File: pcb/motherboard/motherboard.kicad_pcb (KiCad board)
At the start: 4 copper layers, 99.1 x 39.4 mm, 90 parts, among them J1 DC_IN, J10 PSU, J11 HEADER-1x01, J12 HEADER-1x01, J13 USB-LED, J14 EXT, J15 EXT-PW, J16 EXT-I2C, J17 WIFI-GPIO, J2 USB-MINI-B, J3 DB PWR, J4 ICSP-USB, J5 Micro_SD, J6 PSU-SIG, J7 ICSP, J8 FRONT PANEL, J9 DB I/O, SW1 RESET, U1 ATMEGA2560-16AU, U2 DS3231M, U3 ATMEGA8U2-AU, U4 ATWINC1500-MR, U5 74X4050, U6 AP2112K-3.3, U7 74X4050, Y1 16.00 MHz, Y2 16.00 MHz

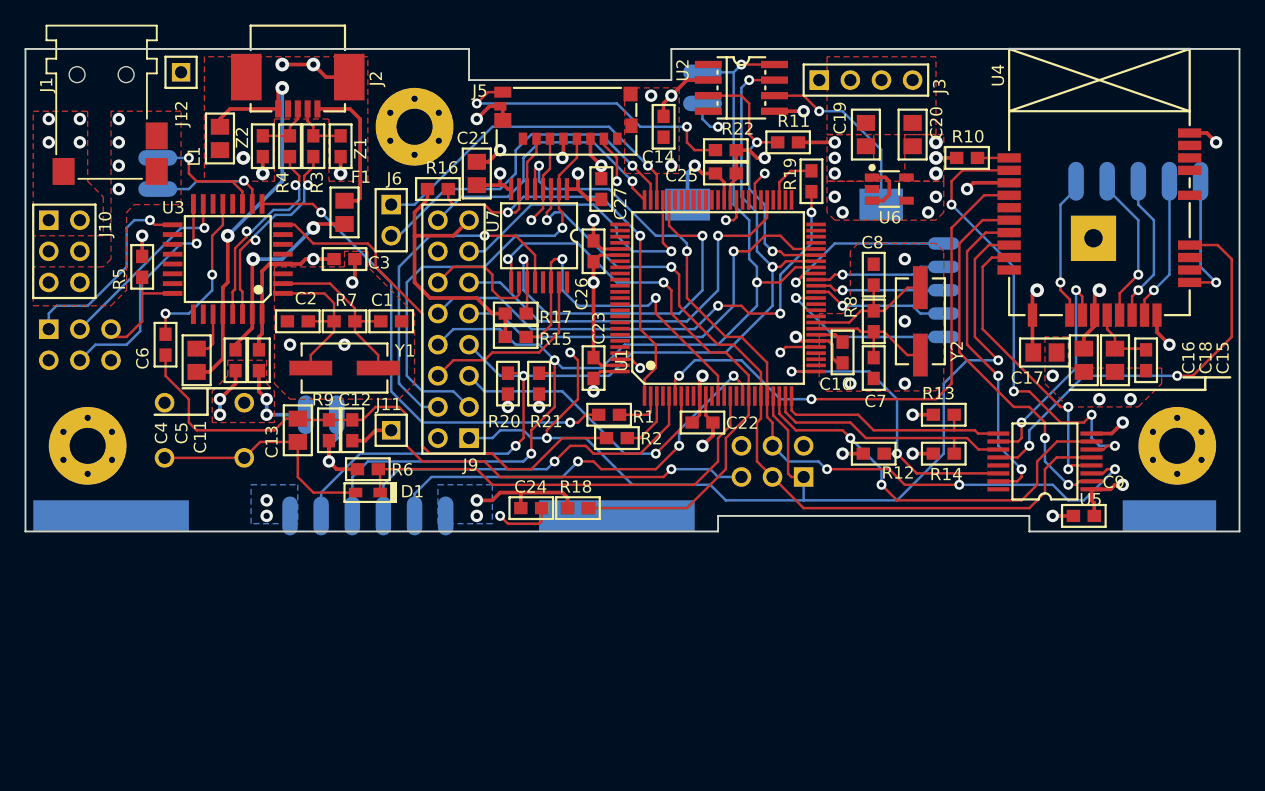
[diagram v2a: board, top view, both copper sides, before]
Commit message: Adjusted page size for motherboard schematic
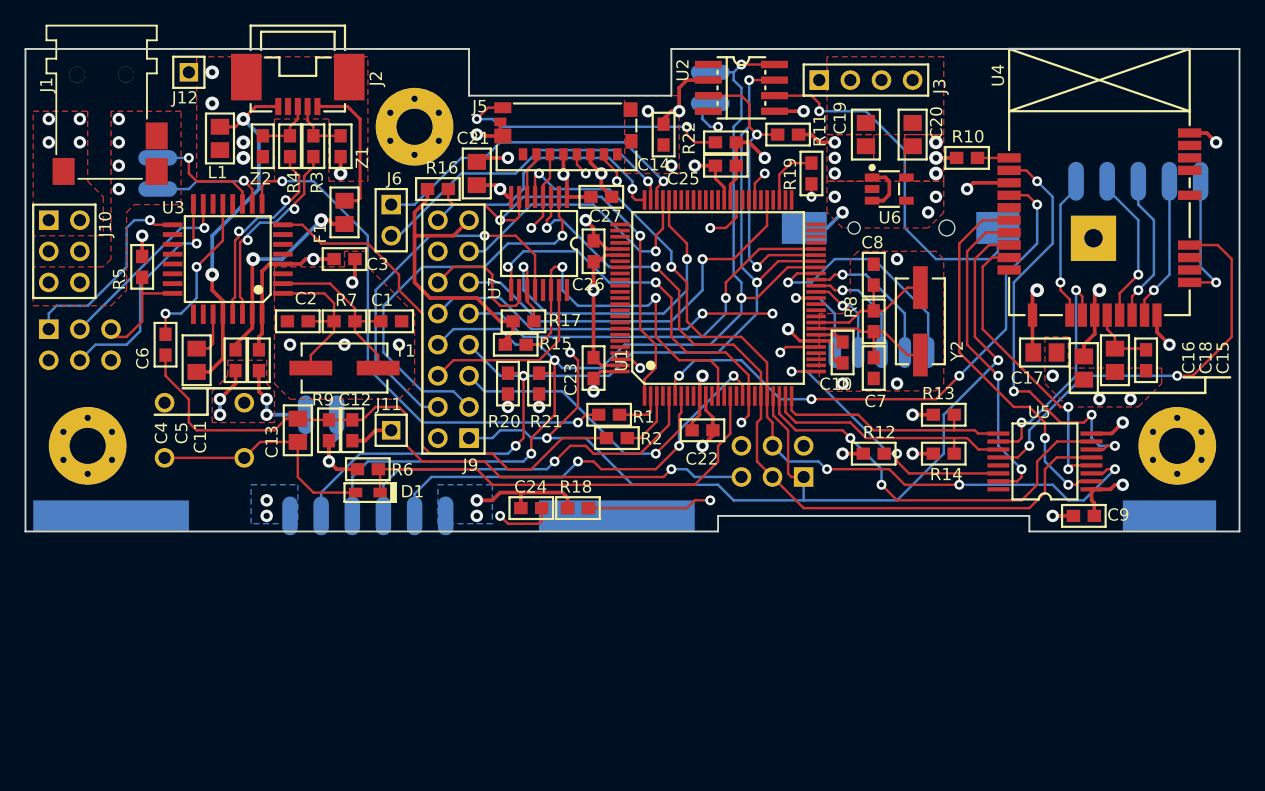
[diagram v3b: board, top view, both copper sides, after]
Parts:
- moved REF** 13.5 mm to (196.2, 108.6)
- moved B1 9.71 mm to (179.1, 99.1)
- moved J14 7.18 mm to (177.8, 109.2), turned to 180 degrees
- moved J5 1.27 mm to (152.4, 88.9)
- moved R17 0.90 mm to (148.6, 106.7)
- moved J16 0.64 mm to (163.8, 87.6)
- moved R11 0.64 mm to (170.2, 91.4)
- moved R19 0.64 mm to (172.1, 94.6)
- moved U7 0.64 mm to (149.9, 100.3)
- moved C14 0.63 mm to (160.0, 91.4)
- moved C16 0.63 mm to (194.3, 110.5)
- moved C22 0.63 mm to (163.2, 115.6)
- moved C25 0.63 mm to (165.1, 94.0)
- moved C27 0.63 mm to (154.9, 96.5), turned to 180 degrees
- moved J12 0.63 mm to (121.3, 86.4)
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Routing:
- net Net-(B1-PadP): track 15.0 -> 30.0 mm
- net /USB Serial/USHLD: track 8.64 -> 1.37 mm
- net /P46: track 14.4 -> 8.53 mm
- net /P42: track 15.3 -> 19.8 mm
- net /Peripherals/CSCK_3V3: track 36.3 -> 40.6 mm, vias 1 -> 2
- net /USB Serial/UGND: track 34.3 -> 30.0 mm
- net +5V: track 63.2 -> 67.4 mm
- net /XDCS: track 32.9 -> 28.9 mm
- net /P45: track 11.1 -> 7.34 mm
- net Net-(R1-Pad1): track 40.3 -> 43.8 mm
- net DVDD: track 49.5 -> 46.7 mm, vias 3 -> 2
- net /Peripherals/WWAKE_3V3: track 38.1 -> 35.4 mm
- net /WCS: track 26.0 -> 23.7 mm
- net /ON_BATT: track 28.7 -> 26.5 mm
- net /KCHG: track 35.6 -> 33.6 mm
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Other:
- outline, holes or cut-outs redrawn
- net class Power: trace_width 0.3048 -> 0.254
- rule trace_min: 0.2 -> 0.2032
- rule via_min_size: 0.4 -> 0.4064

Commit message: Cleanup
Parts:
- removed REF**: VAL**, symbols:SIGNATURE_SILK
- removed REF**: VAL**, symbols:LOGO-OSHW-250
- D1: value DIODE -> 1N4148
- J1: value DC_IN -> -
- J11, J12: value HEADER-1x01 -> PSU-GND
- U4: value ATWINC1500-MR -> ATWINC1500-MR210PB
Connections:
- net Net-(C6-Pad2) renamed /USB Serial/URESET
- net Net-(R1-Pad1) renamed /USB Serial/URXD
- net Net-(R2-Pad1) renamed /USB Serial/UTXD

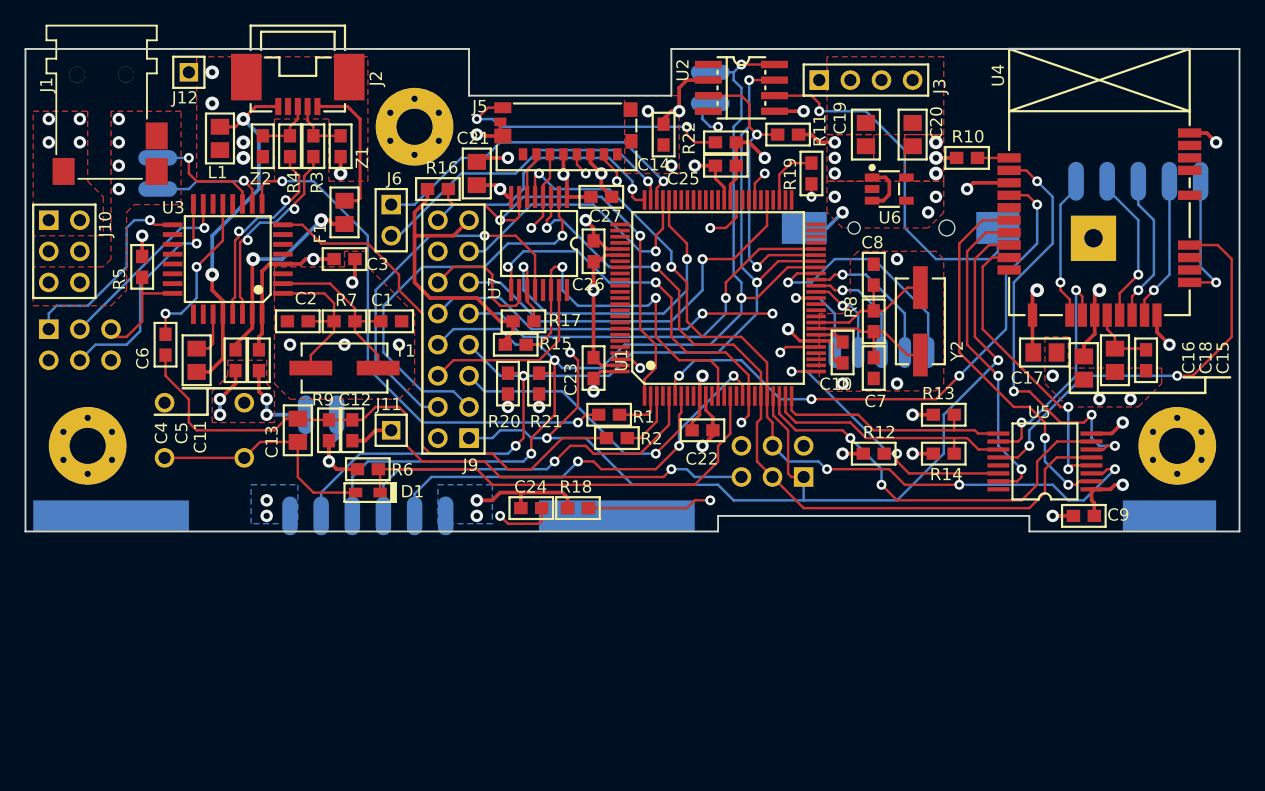
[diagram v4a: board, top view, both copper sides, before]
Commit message: Updated PCB design
+ Completed daughterboard PCB layout.
* Corrected soldermask clerance on front panel pcb.
- Removed input resistor on DIN for RGB lamp board.
* Modified PCB layout for PSU board.
* Updated gerber files.
* Updated schematics pdf, BOM.
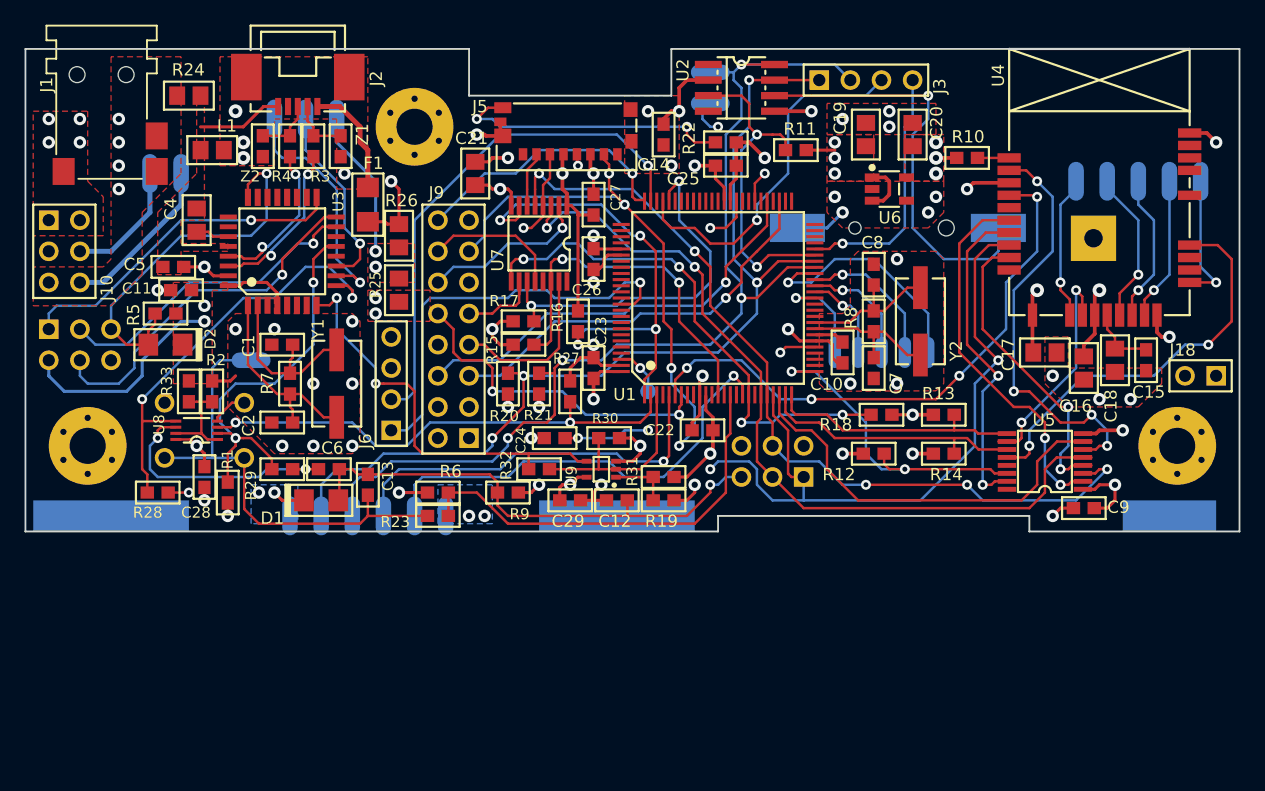
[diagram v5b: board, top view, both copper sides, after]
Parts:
- removed C3: 100nF, smt:C-0603
- removed J12: PSU-GND, conn-header:HDR-M-1x01
- added C28: 100nF, smt:C-0603, F.Cu at (122.6, 119.4)
- added C29: 100nF, smt:C-0603, F.Cu at (152.4, 121.3)
- added D2: CD1206-S01575, smt:D-1206, F.Cu at (119.4, 108.6)
- added J18: DB-C, conn-header:HDR-M-1x02, F.Cu at (203.8, 111.1)
- added R23: 1k, smt:R-0603, F.Cu at (141.6, 122.6)
- added R24: 0, smt:R-0805, F.Cu at (121.3, 88.3)
- added R25: N/A, smt:R-0805, F.Cu at (138.4, 104.1)
- added R26: 0, smt:R-0805, F.Cu at (138.4, 99.7)
- added R27: 10k, smt:R-0603, F.Cu at (152.4, 112.4)
- added R28: N/A, smt:R-0603, F.Cu at (118.7, 120.7)
- added R29: N/A, smt:R-0603, F.Cu at (128.9, 118.7)
- added R30: 10k, smt:R-0603, F.Cu at (155.6, 116.2)
- added R31: 100k, smt:R-0603, F.Cu at (160.0, 119.4)
- added R32: N/A, smt:R-0603, F.Cu at (149.9, 118.7)
- added R33: 1k, smt:R-0603, F.Cu at (121.3, 112.4)
- added TP1: AREF, conn-wire-pads:TEST-POINT-50, B.Cu at (158.8, 112.4)
- added U8: 74LVC2G126DC, smt-sop:VSSOP8, F.Cu at (121.9, 115.6)
- added U9: 74AHC1G126SE-7, smt-sot:SOT-353, F.Cu at (154.9, 118.7)
- B1: footprint conn-power:BC501SM -> conn-power:S8411-45R
- C13: value 1uF -> 100nF; footprint smt:C-0805 -> smt:C-0603
- D1: value 1N4148 -> CD1206-S01575; footprint smt:SOD-323 -> smt:D-1206
- F1: footprint smt:FER-0805 -> smt:FER-1206
- J11: value PSU-GND -> RESET-SW; footprint conn-header:HDR-M-1x01 -> conn-wire-pads:WP-50mil-1x01; moved to B.Cu
- J13: footprint conn-wire-pads:WP-50mil-1x02 -> conn-wire-pads:WP-50mil-1x03
- J3: value DB PWR -> DB-B
- J4: value ICSP-USB -> ICSP-0
- J6: footprint conn-header:HDR-M-1x02 -> conn-header:HDR-M-1x04
- J7: value ICSP -> ICSP-1
- J9: value DB I/O -> DB-A
- R1: value 1k -> 10k
- R19: value 300 -> 1k; footprint smt:C-0603 -> smt:R-0603
- R2: value 1k -> 100k
- U2: value DS3231M -> DS3231MZ
- U3: value ATMEGA8U2-AU -> ATMEGA16U2-AU
- U5, U7: value 74X4050 -> CD74HC4050PWR; footprint smt-sop:SSOP16 -> smt-sop:TSSOP16
- Y1, Y2: footprint crystals:HC49USX -> crystals:smt-CSM-3X-7x4mm
- Z1, Z2: value PGB1010603 -> CG0603MLC-05E
- moved R2 33.2 mm to (123.2, 112.4), turned to 270 degrees
- moved R1 31.8 mm to (124.5, 120.7), turned to 270 degrees
- moved R19 29.3 mm to (160.0, 121.3), turned to 0 degrees
- moved R18 25.9 mm to (177.8, 114.3), turned to 180 degrees
- moved J15 23.4 mm to (119.4, 94.6), turned to 0 degrees
- moved C12 22.3 mm to (156.2, 121.3), turned to 0 degrees
- moved C6 16.8 mm to (132.7, 118.7), turned to 180 degrees
- moved R16 15.7 mm to (153.0, 106.7), turned to 270 degrees
- moved R9 15.5 mm to (147.3, 120.7), turned to 0 degrees
- moved J6 13.3 mm to (137.8, 111.8), turned to 90 degrees
- moved J13 12.9 mm to (130.8, 90.2), turned to 180 degrees
- moved J11 12.8 mm to (126.4, 109.9), turned to 270 degrees
- moved C4 11.4 mm to (121.9, 98.4), turned to 270 degrees
- moved C5 9.16 mm to (120.0, 102.2), turned to 0 degrees
- moved C1 9.09 mm to (128.9, 108.6), turned to 180 degrees
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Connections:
- C11 pad 1: +5V -> UVCC
- C5 pad 1: GND -> /USB Serial/UGND
- C5 pad 2: /USB Serial/UVCC -> /USB Serial/UVCC_IN
- C6 pad 2: /USB Serial/URESET -> /USB Serial/RESET
- D1 pad A: Net-(C13-Pad1) -> /RESET
- D1 pad K: /CFG\~RST -> +5V
- F1 pad 1: /USB Serial/UVCC_IN -> Net-(F1-Pad1)
- F1 pad 2: /USB Serial/UVCC -> /USB Serial/UVCC_IN
- J11 pad 1: GND -> Net-(C13-Pad1)
- J13 pad 1: /USB Serial/LED_TX -> UVCC
- J13 pad 2: /USB Serial/LED_RX -> /USB Serial/LED_TX
- J2 pad 1: /USB Serial/UVCC_IN -> Net-(F1-Pad1)
- J3 pad 1: +5V -> /SDA
- J3 pad 2: +5V -> /SCL
- J3 pad 3: GND -> /A_SHDN
- J3 pad 4: GND -> /KCHG
- J4 pad 2: +5V -> UVCC
- J9 pad 1: /MISO -> +5V
- J9 pad 10: /PIX_CLK -> /DREQ
- J9 pad 11: /PIX_LAMP -> /Peripherals/CMOSI_3V3
- J9 pad 12: /Peripherals/CRST_3V3 -> /Peripherals/CSCK_3V3
- J9 pad 13: /A_SHDN -> /MISO
- J9 pad 14: /PIX_SHDN -> /Peripherals/XDCS_3V3
- J9 pad 2: /Peripherals/CMOSI_3V3 -> +5V
- J9 pad 3: /Peripherals/CSCK_3V3 -> GND
- J9 pad 4: /Peripherals/XDCS_3V3 -> GND
- J9 pad 5: /DREQ -> /PIX_CLK
- J9 pad 6: /Peripherals/CCS_3V3 -> /PIX_LAMP
- J9 pad 7: /SDA -> /Peripherals/CCS_3V3
- J9 pad 8: /SCL -> /PIX_SHDN
- J9 pad 9: /KCHG -> /Peripherals/CRST_3V3
- R1 pad 1: /USB Serial/URXD -> /USB Serial/RESET-M
- R1 pad 2: /RXD0 -> UVCC
- R19 pad 2: /PIX_CLK -> +5V
- R2 pad 1: /USB Serial/UTXD -> GND
- R2 pad 2: /TXD0 -> Net-(R2-Pad2)
- R5 pad 2: +5V -> UVCC
- U1 pad 2: /RXD0 -> /PE0
- U1 pad 3: /TXD0 -> /PE1
- U1 pad 53: Net-(R19-Pad1) -> /PIX_CLK
- U1 pad 73: /LOW_BATT -> Net-(U1-Pad73)
- U1 pad 89: Net-(U1-Pad89) -> /LOW_BATT
- U3 pad 13: /USB Serial/URESET -> /USB Serial/RESET-M
- U3 pad 31: /USB Serial/UVCC -> /USB Serial/UVCC_IN
- U3 pad 32: +5V -> UVCC
- U3 pad 4: +5V -> UVCC
- U3 pad 8: /USB Serial/UTXD -> /USB Serial/URXD
- U3 pad 9: /USB Serial/URXD -> /USB Serial/UTXD
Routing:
- net UVCC: track 0.00 -> 91.3 mm, vias 0 -> 6
- net /PE0: track 0.00 -> 51.9 mm, vias 0 -> 3
- net /USB Serial/RESET-M: track 0.00 -> 32.4 mm, vias 0 -> 2
- net /USB Serial/UGND: track 30.0 -> 7.03 mm, vias 2 -> 0
- net /USB Serial/RESET-USB: track 9.15 -> 31.2 mm, vias 0 -> 1
- net /USB Serial/RESET: track 0.00 -> 20.4 mm, vias 0 -> 2
- net /Peripherals/CSCK_3V3: track 40.6 -> 20.5 mm
- net /USB Serial/UVCC_IN: track 11.7 -> 31.1 mm, vias 0 -> 2
- net Net-(C13-Pad1): track 19.5 -> 38.8 mm
- net /Peripherals/XDCS_3V3: track 30.1 -> 11.3 mm, vias 1 -> 0
- net /USB Serial/UVCC: track 16.9 -> 0.00 mm, vias 2 -> 0
- net /PE1: track 0.00 -> 16.6 mm
- net /RESET: track 71.5 -> 55.6 mm
- net /ON_BATT: track 26.5 -> 42.1 mm
- net /Peripherals/CMOSI_3V3: track 28.4 -> 13.6 mm
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- added copper zone on F.Cu, net /USB Serial/UGND
- added copper zone on F.Cu, net UVCC
- added copper zone on Power, net UVCC
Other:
- rule pad_to_mask_clearance: 0.2 -> 0.1524
- rule via_min_drill: 0.3 -> 0.4064
- rule via_min_size: 0.4064 -> 0.6096
- board text added: "UVCC"
- board text removed: "www.bfrigon.com"

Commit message: Replaced battery holder for Harwin S8411-45R
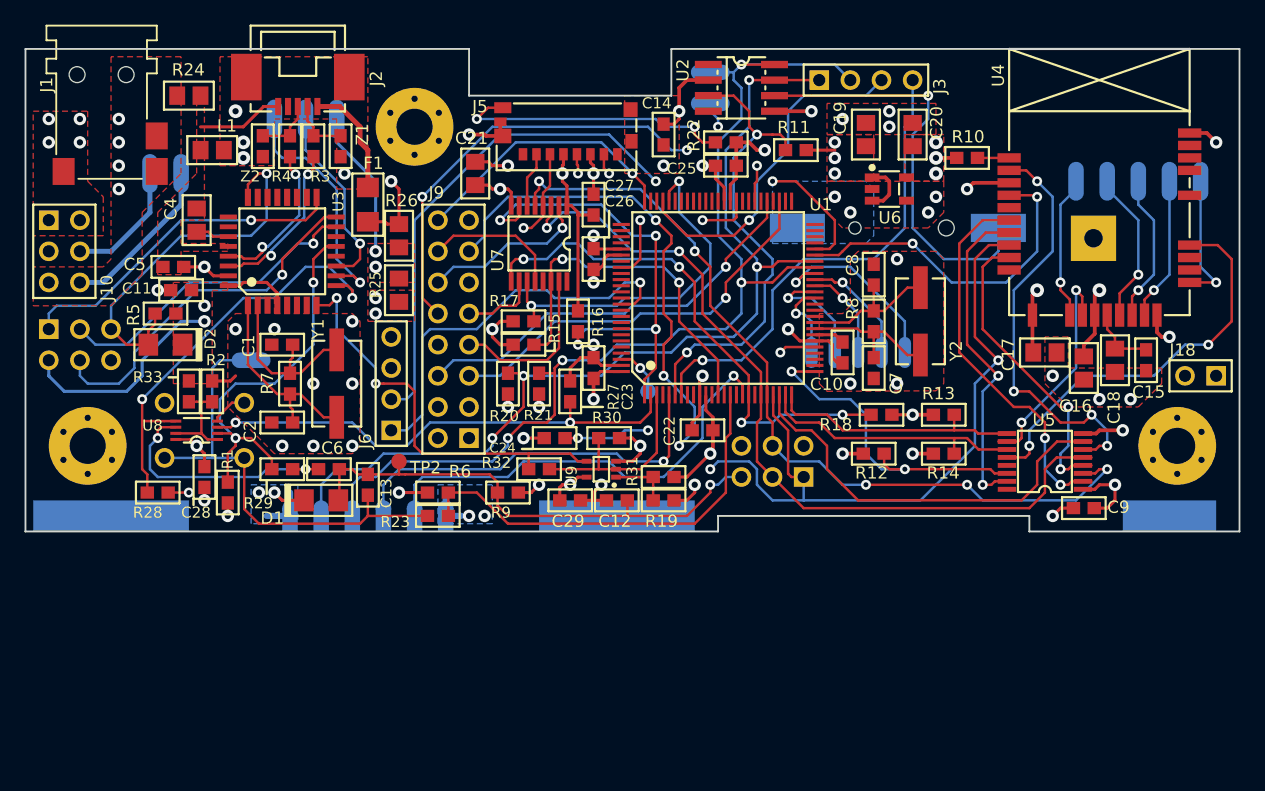
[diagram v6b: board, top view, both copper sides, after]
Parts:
- added TP2: RESET, conn-wire-pads:TEST-POINT-50, F.Cu at (138.4, 118.1)
- C13: value 100nF -> 1uF
- J8: footprint conn-wire-pads:WP-50mil-1x06 -> conn-wire-pads:WP-EDGE-RL-50mil-1x06
- moved J14 1.91 mm to (175.9, 109.2)
- moved J8 1.27 mm to (135.9, 123.8), turned to 180 degrees
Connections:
- U1 pad 45: /RTC_INT -> /WIRQ
- U1 pad 46: /KCHG -> /DREQ
- U1 pad 6: /WIRQ -> /RTC_INT
- U1 pad 7: /DREQ -> /KCHG
- U1 pad 74: /ON_BATT -> Net-(U1-Pad74)
- U1 pad 83: Net-(U1-Pad83) -> /ON_BATT
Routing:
- net /DREQ: track 27.0 -> 52.9 mm, vias 2 -> 3
- net /WIRQ: track 46.8 -> 27.7 mm, vias 4 -> 2
- net /KCHG: track 20.4 -> 39.1 mm
- net /RTC_INT: track 26.8 -> 38.2 mm
- net /MISO: track 102.5 -> 109.9 mm
- net /ON_BATT: track 42.1 -> 49.0 mm, vias 1 -> 2
- net /P42: track 19.8 -> 15.7 mm
- net +5V: track 66.8 -> 69.8 mm
- net /P43: track 11.9 -> 9.39 mm
- net /P45: track 7.34 -> 9.63 mm
- net /PIX_SHDN: track 46.3 -> 44.3 mm
- net /P46: track 8.53 -> 6.62 mm
- net /P44: track 9.45 -> 7.55 mm
- net /LOW_BATT: track 34.1 -> 32.6 mm
- net /A_SHDN: track 29.5 -> 28.2 mm
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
